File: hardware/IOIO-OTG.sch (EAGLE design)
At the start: 58 parts, among them Q1 IRLML2244, Q2 2N7002PW, Q3 AO3404A, U1 PIC24FJ256GB206, U14 SWITCH_SPDT, U2 TPS62133RGTT, U3 VREG_MIC5216

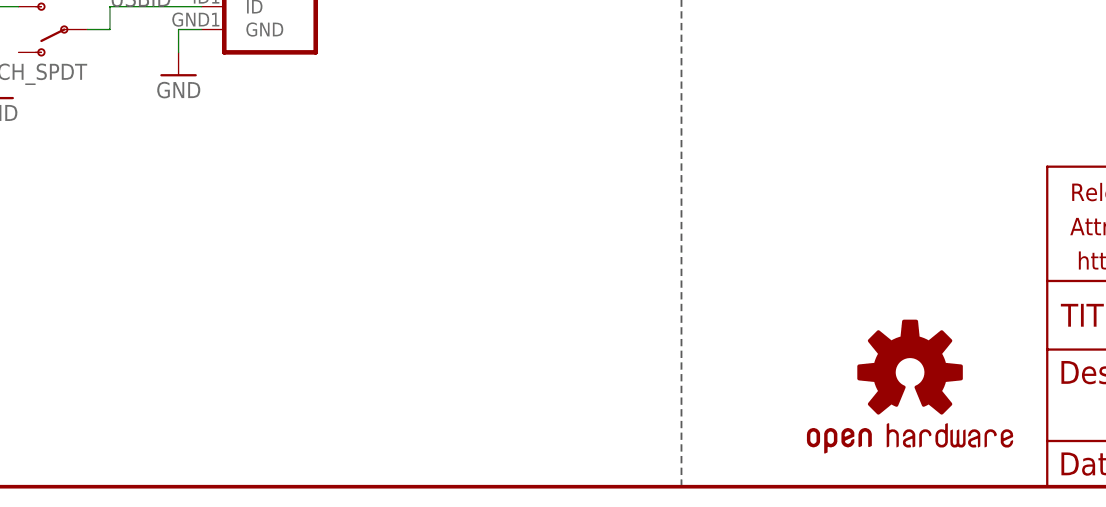
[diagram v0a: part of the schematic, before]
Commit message: moved to SFE logo
both mini flame on top, and backside name/flame
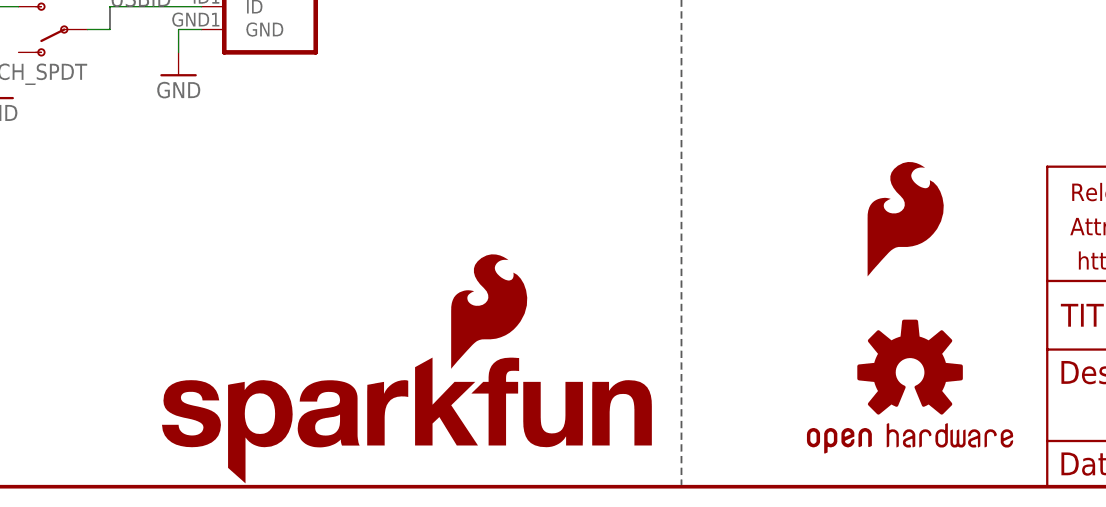
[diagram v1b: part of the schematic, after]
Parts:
- added LOGO2: SFE_LOGO_FLAME.1_INCH, SparkFun-Aesthetics:SFE_LOGO_FLAME.1_INCH
- added LOGO4: SFE_LOGO_NAME_FLAME.1_INCH, SparkFun-Aesthetics:SFE_LOGO_NAME_FLAME.1_INCH
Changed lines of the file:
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@@
 <grid distance="0.1" unitdist="inch" unit="inch" style="lines" multiple="1" display="no" altdistance="0.01" altunitdist="inch" altunit="inch"/>
 <layers>
-<layer number="1" name="Top" color="4" fill="1" visible="no" active="no"/>
-<layer number="2" name="Route2" color="1" fill="3" visible="no" active="no"/>
-<layer number="3" name="Route3" color="4" fill="3" visible="no" active="no"/>
-<layer number="4" name="Route4" color="1" fill="4" visible="no" active="no"/>
-<layer number="5" name="Route5" color="4" fill="4" visible="no" active="no"/>
-<layer number="6" name="Route6" color="1" fill="8" visible="no" active="no"/>
-<layer number="7" name="Route7" color="4" fill="8" visible="no" active="no"/>
-<layer number="8" name="Route8" color="1" fill="2" visible="no" active="no"/>
-<layer number="9" name="Route9" color="4" fill="2" visible="no" active="no"/>
-<layer number="10" name="Route10" color="1" fill="7" visible="no" active="no"/>
-<layer number="11" name="Route11" color="4" fill="7" visible="no" active="no"/>
-<layer number="12" name="Route12" color="1" fill="5" visible="no" active="no"/>
-<layer number="13" name="Route13" color="4" fill="5" visible="no" active="no"/>
-<layer number="14" name="Route14" color="1" fill="6" visible="no" active="no"/>
-<layer number="15" name="Route15" color="4" fill="6" visible="no" active="no"/>
-<layer number="16" name="Bottom" color="1" fill="1" visible="no" active="no"/>
-<layer number="17" name="Pads" color="2" fill="1" visible="no" active="no"/>
-<layer number="18" name="Vias" color="2" fill="1" visible="no" active="no"/>
-<layer number="19" name="Unrouted" color="6" fill="1" visible="no" active="no"/>
-<layer number="20" name="Dimension" color="15" fill="1" visible="no" active="no"/>
-<layer number="21" name="tPlace" color="16" fill="1" visible="no" active="no"/>
-<layer number="22" name="bPlace" color="14" fill="1" visible="no" active="no"/>
-<layer number="23" name="tOrigins" color="15" fill="1" visible="no" active="no"/>
-<layer number="24" name="bOrigins" color="15" fill="1" visible="no" active="no"/>
-<layer number="25" name="tNames" color="7" fill="1" visible="no" active="no"/>
-<layer number="26" name="bNames" color="3" fill="1" visible="no" active="no"/>
-<layer number="27" name="tValues" color="7" fill="1" visible="no" active="no"/>
-<layer number="28" name="bValues" color="7" fill="1" visible="no" active="no"/>
+<layer number="1" name="Top" color="4" fill="1" visible="yes" active="no"/>
+<layer number="2" name="Route2" color="1" fill="3" visible="yes" active="no"/>
+<layer number="3" name="Route3" color="4" fill="3" visible="yes" active="no"/>
+<layer number="4" name="Route4" color="1" fill="4" visible="yes" active="no"/>
+<layer number="5" name="Route5" color="4" fill="4" visible="yes" active="no"/>
+<layer number="6" name="Route6" color="1" fill="8" visible="yes" active="no"/>
+<layer number="7" name="Route7" color="4" fill="8" visible="yes" active="no"/>
+<layer number="8" name="Route8" color="1" fill="2" visible="yes" active="no"/>
+<layer number="9" name="Route9" color="4" fill="2" visible="yes" active="no"/>
+<layer number="10" name="Route10" color="1" fill="7" visible="yes" active="no"/>
+<layer number="11" name="Route11" color="4" fill="7" visible="yes" active="no"/>
+<layer number="12" name="Route12" color="1" fill="5" visible="yes" active="no"/>
+<layer number="13" name="Route13" color="4" fill="5" visible="yes" active="no"/>
+<layer number="14" name="Route14" color="1" fill="6" visible="yes" active="no"/>
+<layer number="15" name="Route15" color="4" fill="6" visible="yes" active="no"/>
+<layer number="16" name="Bottom" color="1" fill="1" visible="yes" active="no"/>
+<layer number="17" name="Pads" color="2" fill="1" visible="yes" active="no"/>
+<layer number="18" name="Vias" color="2" fill="1" visible="yes" active="no"/>
+<layer number="19" name="Unrouted" color="6" fill="1" visible="yes" active="no"/>
+<layer number="20" name="Dimension" color="15" fill="1" visible="yes" active="no"/>
+<layer number="21" name="tPlace" color="16" fill="1" visible="yes" active="no"/>
+<layer number="22" name="bPlace" color="14" fill="1" visible="yes" active="no"/>
+<layer number="23" name="tOrigins" color="15" fill="1" visible="yes" active="no"/>
+<layer number="24" name="bOrigins" color="15" fill="1" visible="yes" active="no"/>
+<layer number="25" name="tNames" color="7" fill="1" visible="yes" active="no"/>
+<layer number="26" name="bNames" color="3" fill="1" visible="yes" active="no"/>
+<layer number="27" name="tValues" color="7" fill="1" visible="yes" active="no"/>
+<layer number="28" name="bValues" color="7" fill="1" visible="yes" active="no"/>
 <layer number="29" name="tStop" color="7" fill="3" visible="no" active="no"/>
 <layer number="30" name="bStop" color="3" fill="6" visible="no" active="no"/>
@@
 <layer number="35" name="tGlue" color="7" fill="4" visible="no" active="no"/>
 <layer number="36" name="bGlue" color="3" fill="5" visible="no" active="no"/>
-<layer number="37" name="tTest" color="7" fill="1" visible="no" active="no"/>
-<layer number="38" name="bTest" color="3" fill="1" visible="no" active="no"/>
+<layer number="37" name="tTest" color="7" fill="1" visible="yes" active="no"/>
+<layer number="38" name="bTest" color="3" fill="1" visible="yes" active="no"/>
 <layer number="39" name="tKeepout" color="4" fill="11" visible="no" active="no"/>
 <layer number="40" name="bKeepout" color="1" fill="11" visible="no" active="no"/>
@@
 <layer number="44" name="Drills" color="7" fill="1" visible="no" active="no"/>
 <layer number="45" name="Holes" color="7" fill="1" visible="no" active="no"/>
-<layer number="46" name="Milling" color="3" fill="1" visible="no" active="no"/>
-<layer number="47" name="Measures" color="7" fill="1" visible="no" active="no"/>
-<layer number="48" name="Document" color="7" fill="1" visible="no" active="no"/>
-<layer number="49" name="Reference" color="7" fill="1" visible="no" active="no"/>
-<layer number="50" name="dxf" color="7" fill="1" visible="no" active="no"/>
-<layer number="51" name="tDocu" color="6" fill="1" visible="no" active="no"/>
-<layer number="52" name="bDocu" color="7" fill="1" visible="no" active="no"/>
-<layer number="53" name="tGND_GNDA" color="7" fill="9" visible="no" active="no"/>
-<layer number="54" name="bGND_GNDA" color="1" fill="9" visible="no" active="no"/>
-<layer number="56" name="wert" color="7" fill="1" visible="no" active="no"/>
-<layer number="57" name="tCAD" color="7" fill="1" visible="no" active="no"/>
-<layer number="59" name="tCarbon" color="7" fill="1" visible="no" active="no"/>
-<layer number="60" name="bCarbon" color="7" fill="1" visible="no" active="no"/>
+<layer number="46" name="Milling" color="3" fill="1" visible="yes" active="no"/>
+<layer number="47" name="Measures" color="7" fill="1" visible="yes" active="no"/>
+<layer number="48" name="Document" color="7" fill="1" visible="yes" active="no"/>
+<layer number="49" name="Reference" color="7" fill="1" visible="yes" active="no"/>
+<layer number="50" name="dxf" color="7" fill="1" visible="yes" active="no"/>
+<layer number="51" name="tDocu" color="6" fill="1" visible="yes" active="no"/>
+<layer number="52" name="bDocu" color="7" fill="1" visible="yes" active="no"/>
+<layer number="53" name="tGND_GNDA" color="7" fill="9" visible="yes" active="no"/>
+<layer number="54" name="bGND_GNDA" color="1" fill="9" visible="yes" active="no"/>
+<layer number="56" name="wert" color="7" fill="1" visible="yes" active="no"/>
+<layer number="57" name="tCAD" color="7" fill="1" visible="yes" active="no"/>
+<layer number="59" name="tCarbon" color="7" fill="1" visible="yes" active="no"/>
+<layer number="60" name="bCarbon" color="7" fill="1" visible="yes" active="no"/>
 <layer number="90" name="Modules" color="5" fill="1" visible="yes" active="yes"/>
 <layer number="91" name="Nets" color="2" fill="1" visible="yes" active="yes"/>
@@
 <part name="LOGO1" library="SparkFun-Aesthetics" deviceset="OSHW-LOGO" device="S" value="OSHW-LOGOS"/>
 <part name="FRAME2" library="SparkFun-Aesthetics" deviceset="FRAME-LEDGER" device=""/>
+<part name="LOGO2" library="SparkFun-Aesthetics" deviceset="SFE_LOGO_FLAME" device=".1_INCH"/>
+<part name="LOGO4" library="SparkFun-Aesthetics" deviceset="SFE_LOGO_NAME_FLAME" device=".1_INCH"/>
 </parts>
 <sheets>
@@
 <instance part="FRAME2" gate="G$1" x="0" y="0"/>
 <instance part="FRAME2" gate="G$2" x="330.2" y="0"/>
+<instance part="LOGO2" gate="G$1" x="309.88" y="22.86"/>
+<instance part="LOGO4" gate="G$1" x="231.14" y="0"/>
 </instances>
 <busses>

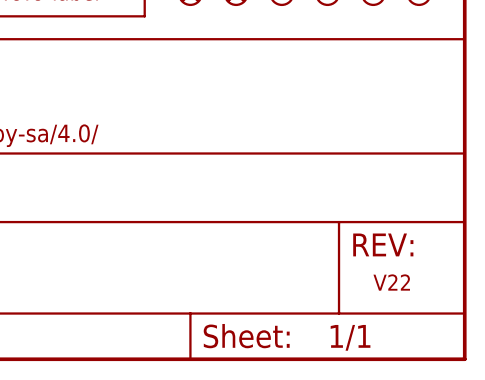
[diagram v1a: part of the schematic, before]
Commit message: DFM routing for TPS chip
-added tRestrict to separate pads on TPS chip.
-changed copper to v22b
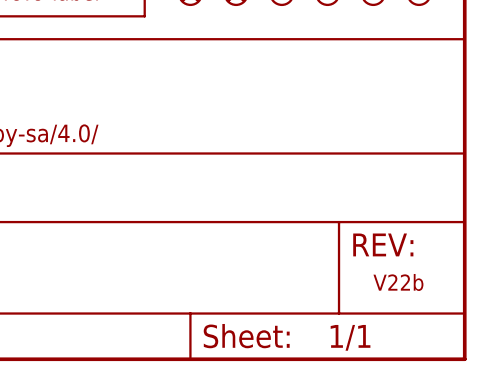
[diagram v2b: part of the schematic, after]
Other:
- note added: "V22b"
- note removed: "V22"
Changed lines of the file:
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@@
 <grid distance="0.1" unitdist="inch" unit="inch" style="lines" multiple="1" display="no" altdistance="0.01" altunitdist="inch" altunit="inch"/>
 <layers>
-<layer number="1" name="Top" color="4" fill="1" visible="yes" active="no"/>
-<layer number="2" name="Route2" color="1" fill="3" visible="yes" active="no"/>
-<layer number="3" name="Route3" color="4" fill="3" visible="yes" active="no"/>
-<layer number="4" name="Route4" color="1" fill="4" visible="yes" active="no"/>
-<layer number="5" name="Route5" color="4" fill="4" visible="yes" active="no"/>
-<layer number="6" name="Route6" color="1" fill="8" visible="yes" active="no"/>
-<layer number="7" name="Route7" color="4" fill="8" visible="yes" active="no"/>
-<layer number="8" name="Route8" color="1" fill="2" visible="yes" active="no"/>
-<layer number="9" name="Route9" color="4" fill="2" visible="yes" active="no"/>
-<layer number="10" name="Route10" color="1" fill="7" visible="yes" active="no"/>
-<layer number="11" name="Route11" color="4" fill="7" visible="yes" active="no"/>
-<layer number="12" name="Route12" color="1" fill="5" visible="yes" active="no"/>
-<layer number="13" name="Route13" color="4" fill="5" visible="yes" active="no"/>
-<layer number="14" name="Route14" color="1" fill="6" visible="yes" active="no"/>
-<layer number="15" name="Route15" color="4" fill="6" visible="yes" active="no"/>
-<layer number="16" name="Bottom" color="1" fill="1" visible="yes" active="no"/>
-<layer number="17" name="Pads" color="2" fill="1" visible="yes" active="no"/>
-<layer number="18" name="Vias" color="2" fill="1" visible="yes" active="no"/>
-<layer number="19" name="Unrouted" color="6" fill="1" visible="yes" active="no"/>
-<layer number="20" name="Dimension" color="15" fill="1" visible="yes" active="no"/>
-<layer number="21" name="tPlace" color="16" fill="1" visible="yes" active="no"/>
-<layer number="22" name="bPlace" color="14" fill="1" visible="yes" active="no"/>
-<layer number="23" name="tOrigins" color="15" fill="1" visible="yes" active="no"/>
-<layer number="24" name="bOrigins" color="15" fill="1" visible="yes" active="no"/>
-<layer number="25" name="tNames" color="7" fill="1" visible="yes" active="no"/>
-<layer number="26" name="bNames" color="3" fill="1" visible="yes" active="no"/>
-<layer number="27" name="tValues" color="7" fill="1" visible="yes" active="no"/>
-<layer number="28" name="bValues" color="7" fill="1" visible="yes" active="no"/>
+<layer number="1" name="Top" color="4" fill="1" visible="no" active="no"/>
+<layer number="2" name="Route2" color="1" fill="3" visible="no" active="no"/>
+<layer number="3" name="Route3" color="4" fill="3" visible="no" active="no"/>
+<layer number="4" name="Route4" color="1" fill="4" visible="no" active="no"/>
+<layer number="5" name="Route5" color="4" fill="4" visible="no" active="no"/>
+<layer number="6" name="Route6" color="1" fill="8" visible="no" active="no"/>
+<layer number="7" name="Route7" color="4" fill="8" visible="no" active="no"/>
+<layer number="8" name="Route8" color="1" fill="2" visible="no" active="no"/>
+<layer number="9" name="Route9" color="4" fill="2" visible="no" active="no"/>
+<layer number="10" name="Route10" color="1" fill="7" visible="no" active="no"/>
+<layer number="11" name="Route11" color="4" fill="7" visible="no" active="no"/>
+<layer number="12" name="Route12" color="1" fill="5" visible="no" active="no"/>
+<layer number="13" name="Route13" color="4" fill="5" visible="no" active="no"/>
+<layer number="14" name="Route14" color="1" fill="6" visible="no" active="no"/>
+<layer number="15" name="Route15" color="4" fill="6" visible="no" active="no"/>
+<layer number="16" name="Bottom" color="1" fill="1" visible="no" active="no"/>
+<layer number="17" name="Pads" color="2" fill="1" visible="no" active="no"/>
+<layer number="18" name="Vias" color="2" fill="1" visible="no" active="no"/>
+<layer number="19" name="Unrouted" color="6" fill="1" visible="no" active="no"/>
+<layer number="20" name="Dimension" color="15" fill="1" visible="no" active="no"/>
+<layer number="21" name="tPlace" color="16" fill="1" visible="no" active="no"/>
+<layer number="22" name="bPlace" color="14" fill="1" visible="no" active="no"/>
+<layer number="23" name="tOrigins" color="15" fill="1" visible="no" active="no"/>
+<layer number="24" name="bOrigins" color="15" fill="1" visible="no" active="no"/>
+<layer number="25" name="tNames" color="7" fill="1" visible="no" active="no"/>
+<layer number="26" name="bNames" color="3" fill="1" visible="no" active="no"/>
+<layer number="27" name="tValues" color="7" fill="1" visible="no" active="no"/>
+<layer number="28" name="bValues" color="7" fill="1" visible="no" active="no"/>
 <layer number="29" name="tStop" color="7" fill="3" visible="no" active="no"/>
 <layer number="30" name="bStop" color="3" fill="6" visible="no" active="no"/>
@@
 <layer number="35" name="tGlue" color="7" fill="4" visible="no" active="no"/>
 <layer number="36" name="bGlue" color="3" fill="5" visible="no" active="no"/>
-<layer number="37" name="tTest" color="7" fill="1" visible="yes" active="no"/>
-<layer number="38" name="bTest" color="3" fill="1" visible="yes" active="no"/>
+<layer number="37" name="tTest" color="7" fill="1" visible="no" active="no"/>
+<layer number="38" name="bTest" color="3" fill="1" visible="no" active="no"/>
 <layer number="39" name="tKeepout" color="4" fill="11" visible="no" active="no"/>
 <layer number="40" name="bKeepout" color="1" fill="11" visible="no" active="no"/>
@@
 <layer number="44" name="Drills" color="7" fill="1" visible="no" active="no"/>
 <layer number="45" name="Holes" color="7" fill="1" visible="no" active="no"/>
-<layer number="46" name="Milling" color="3" fill="1" visible="yes" active="no"/>
-<layer number="47" name="Measures" color="7" fill="1" visible="yes" active="no"/>
-<layer number="48" name="Document" color="7" fill="1" visible="yes" active="no"/>
-<layer number="49" name="Reference" color="7" fill="1" visible="yes" active="no"/>
-<layer number="50" name="dxf" color="7" fill="1" visible="yes" active="no"/>
-<layer number="51" name="tDocu" color="6" fill="1" visible="yes" active="no"/>
-<layer number="52" name="bDocu" color="7" fill="1" visible="yes" active="no"/>
-<layer number="53" name="tGND_GNDA" color="7" fill="9" visible="yes" active="no"/>
-<layer number="54" name="bGND_GNDA" color="1" fill="9" visible="yes" active="no"/>
-<layer number="56" name="wert" color="7" fill="1" visible="yes" active="no"/>
-<layer number="57" name="tCAD" color="7" fill="1" visible="yes" active="no"/>
-<layer number="59" name="tCarbon" color="7" fill="1" visible="yes" active="no"/>
-<layer number="60" name="bCarbon" color="7" fill="1" visible="yes" active="no"/>
+<layer number="46" name="Milling" color="3" fill="1" visible="no" active="no"/>
+<layer number="47" name="Measures" color="7" fill="1" visible="no" active="no"/>
+<layer number="48" name="Document" color="7" fill="1" visible="no" active="no"/>
+<layer number="49" name="Reference" color="7" fill="1" visible="no" active="no"/>
+<layer number="50" name="dxf" color="7" fill="1" visible="no" active="no"/>
+<layer number="51" name="tDocu" color="6" fill="1" visible="no" active="no"/>
+<layer number="52" name="bDocu" color="7" fill="1" visible="no" active="no"/>
+<layer number="53" name="tGND_GNDA" color="7" fill="9" visible="no" active="no"/>
+<layer number="54" name="bGND_GNDA" color="1" fill="9" visible="no" active="no"/>
+<layer number="56" name="wert" color="7" fill="1" visible="no" active="no"/>
+<layer number="57" name="tCAD" color="7" fill="1" visible="no" active="no"/>
+<layer number="59" name="tCarbon" color="7" fill="1" visible="no" active="no"/>
+<layer number="60" name="bCarbon" color="7" fill="1" visible="no" active="no"/>
 <layer number="90" name="Modules" color="5" fill="1" visible="yes" active="yes"/>
 <layer number="91" name="Nets" color="2" fill="1" visible="yes" active="yes"/>
@@
 <text x="11.43" y="186.436" size="3.81" layer="97">MCU</text>
 <wire x1="289.56" y1="200.66" x2="431.8" y2="200.66" width="0.2032" layer="97" style="shortdash"/>
-<text x="421.64" y="7.62" size="1.778" layer="94" font="vector">V22</text>
+<text x="421.64" y="7.62" size="1.778" layer="94" font="vector">V22b</text>
 </plain>
 <instances>

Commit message: Schematic Cleanup
flags, spacing, revisor
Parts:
- JP2: value (none) -> 3.3V
- renumbered LED1 to D3, LED2 to D5, U$2 to JP20, U14 to S1
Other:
- note added: "revised by A.Weiss, Pete Lewis"
- note removed: "revised by A.Weiss"
- moved on the sheet: C10, C11, C6, C7, C8, C9, D2, JP19, JP3, L2, Q1, Q2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
